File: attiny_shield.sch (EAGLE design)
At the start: 13 parts, among them IC1 TINY13-20PU

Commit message: - clean-up
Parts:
- 85_V_84: device SparkFun-Switches:SWITCH-SPDT-SMD-AYZ0202 -> PianoPiano:SPARKFUN-SWITCHES_SWITCH-SPDT-SMD-AYZ0202
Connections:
- removed net N$9: C1.1, PROGRAM_SWITCH.S
- new net N$1: C1.1, PROGRAM_SWITCH.O
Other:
- note added: "Arduino Uno R3"
- moved on the sheet: C1, J5, J6, J7, J8

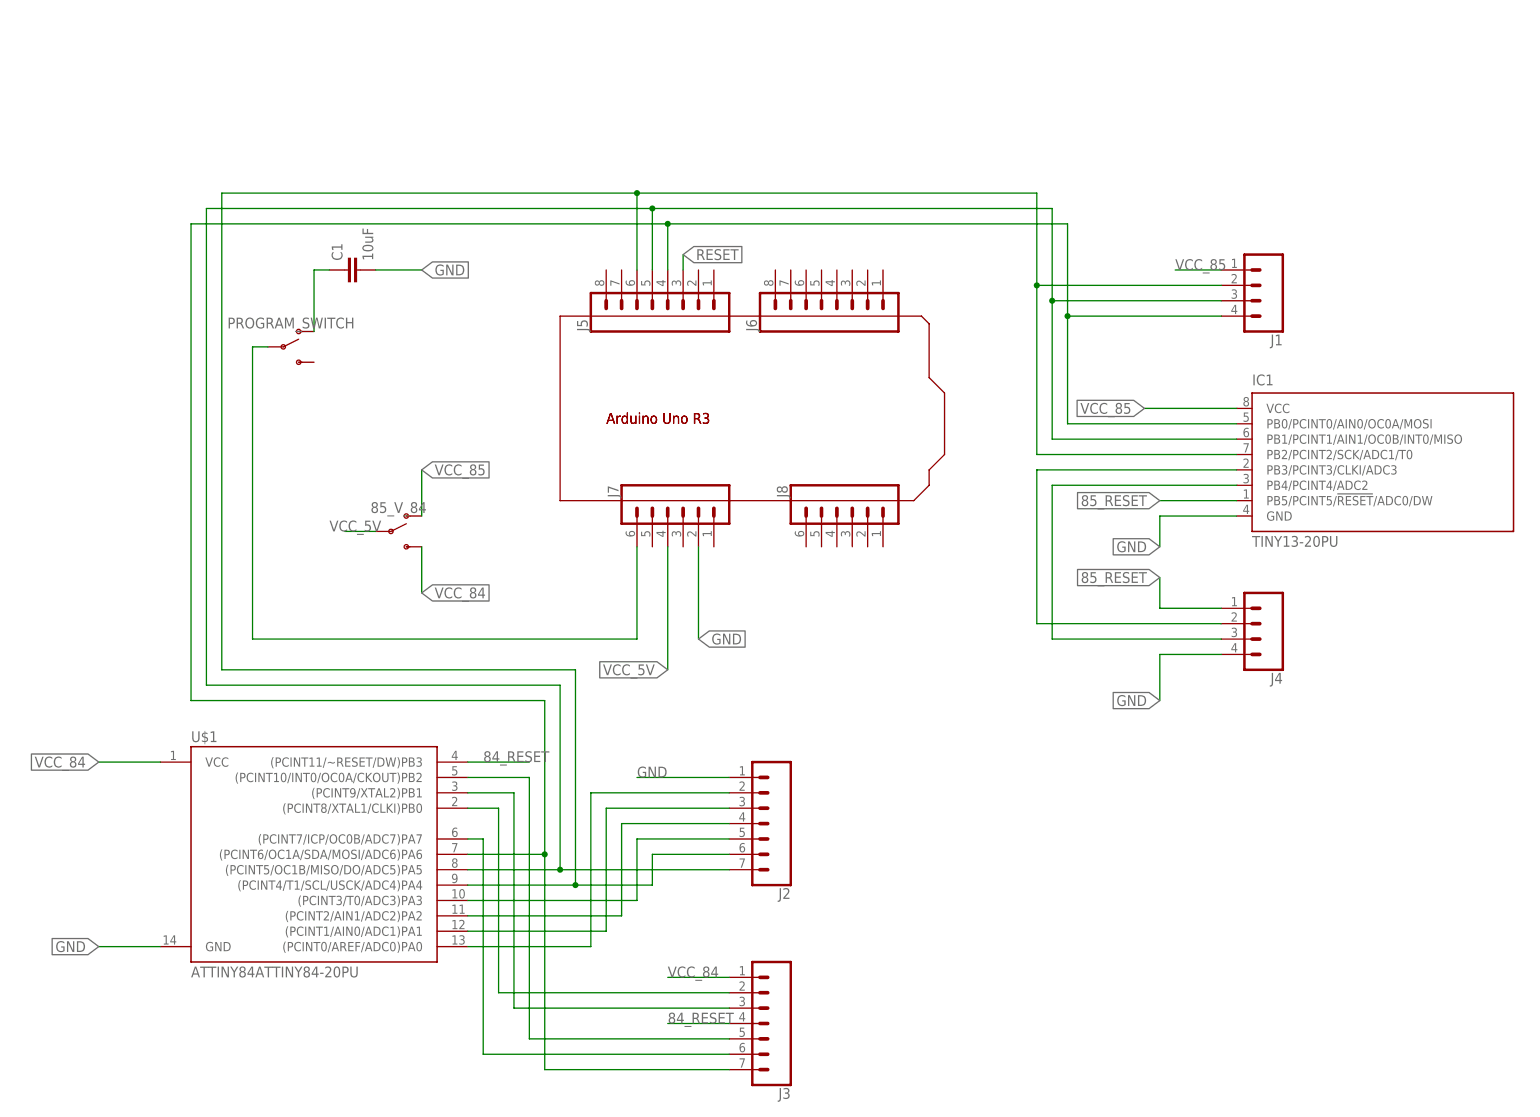
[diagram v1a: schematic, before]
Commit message: added caps and pull-ups. added reset button.
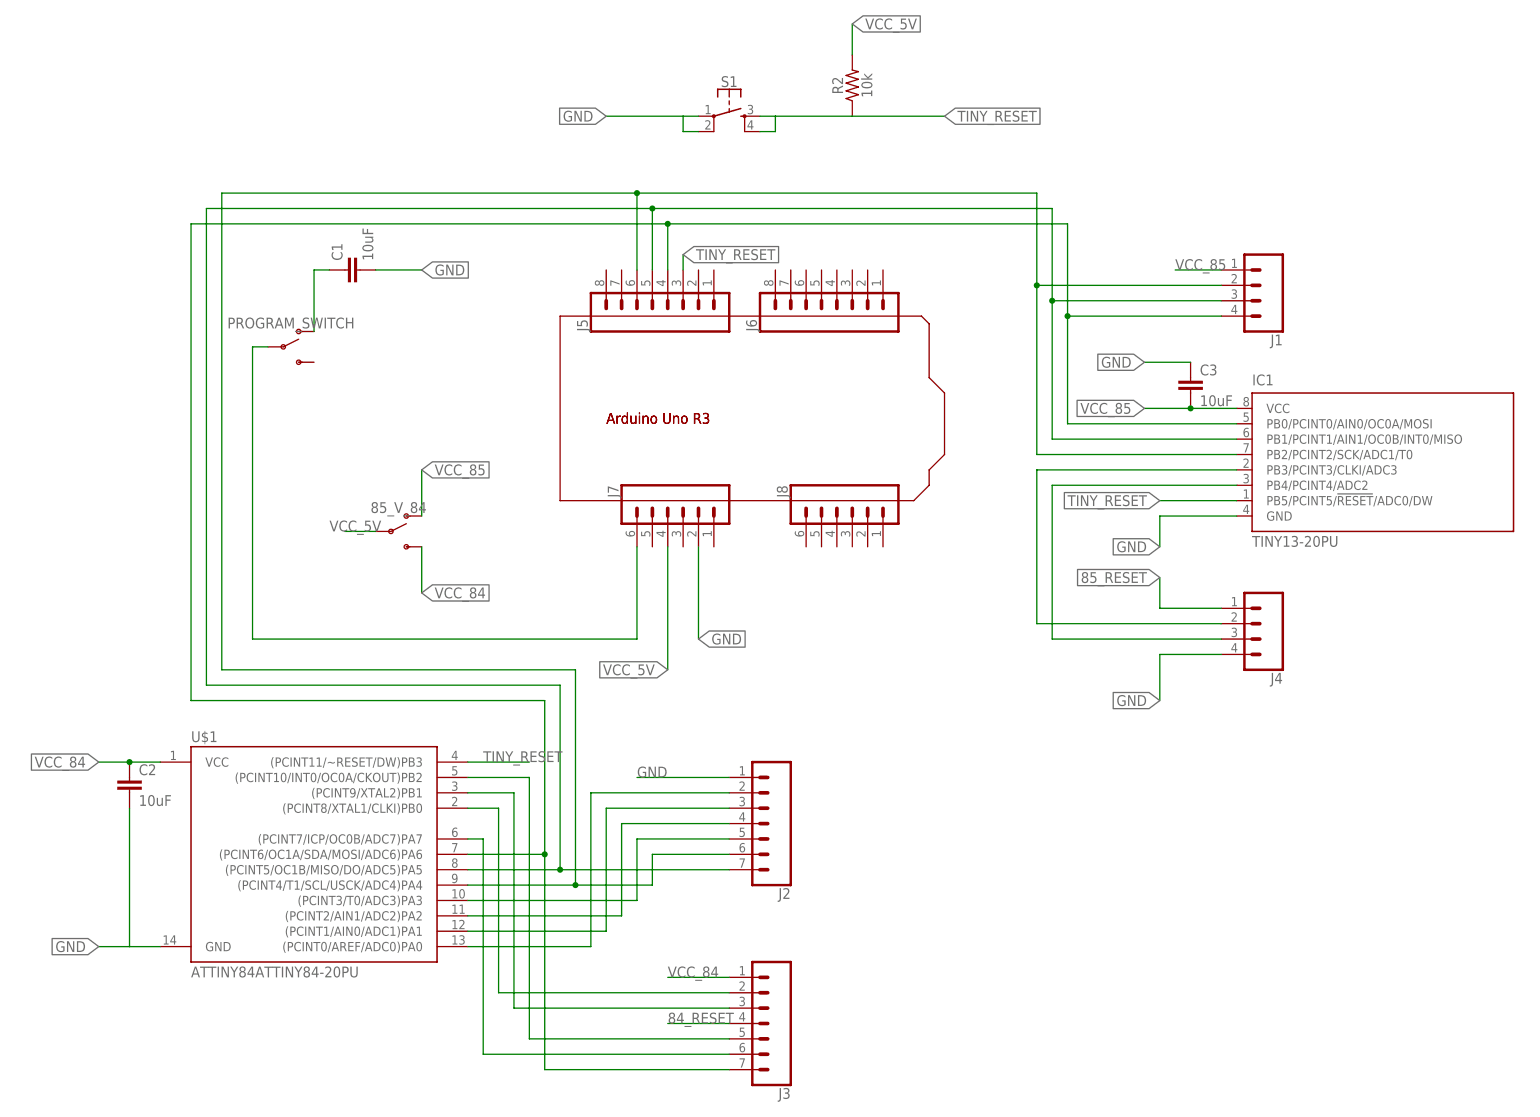
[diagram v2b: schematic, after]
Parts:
- added C2, C3: 10uF, SparkFun-Capacitors:10UF-0805-10V-10%
- added R2: 10k, PianoPiano:SPARKFUN-RESISTORS_10KOHM-0603-1/10W-1%
- added S1: (no value), PianoPiano:SPARKFUN-SWITCHES_MOMENTARY-SWITCH-SPST-2-SMD-5.2MM
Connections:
- removed net RESET: J5.3
- new net TINY_RESET: IC1.PB5/PCINT5/!RESET!/ADC0/DW, J5.3, R2.1, S1.3, S1.4, U$1.(PCINT11/~RESET/DW)PB3
- net 84_RESET: no longer U$1.(PCINT11/~RESET/DW)PB3
- net 85_RESET: no longer IC1.PB5/PCINT5/!RESET!/ADC0/DW
- net GND: now also C2.2, C3.1, S1.1, S1.2
- net VCC_5V: now also R2.2
- net VCC_84: now also C2.1
- net VCC_85: now also C3.2
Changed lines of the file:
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@@
 <drawing>
 <settings>
-<setting alwaysvectorfont="yes"/>
+<setting alwaysvectorfont="no"/>
 <setting verticaltext="up"/>
 </settings>
@@
 <part name="J7" library="SparkFun-Connectors" library_urn="urn:adsk.eagle:library:513" deviceset="CONN_06" device="SILK_FEMALE_PTH" package3d_urn="urn:adsk.eagle:package:38009/1"/>
 <part name="J8" library="SparkFun-Connectors" library_urn="urn:adsk.eagle:library:513" deviceset="CONN_06" device="SILK_FEMALE_PTH" package3d_urn="urn:adsk.eagle:package:38009/1"/>
+<part name="S1" library="PianoPiano" library_urn="urn:adsk.eagle:library:1762222" deviceset="SPARKFUN-SWITCHES_MOMENTARY-SWITCH-SPST-2" device="-SMD-5.2MM" package3d_urn="urn:adsk.eagle:package:1762345/2"/>
+<part name="R2" library="PianoPiano" library_urn="urn:adsk.eagle:library:1762222" deviceset="SPARKFUN-RESISTORS_10KOHM" device="-0603-1/10W-1%" package3d_urn="urn:adsk.eagle:package:1762339/2" value="10k"/>
+<part name="C2" library="SparkFun-Capacitors" deviceset="10UF" device="-0805-10V-10%" value="10uF"/>
+<part name="C3" library="SparkFun-Capacitors" deviceset="10UF" device="-0805-10V-10%" value="10uF"/>
 </parts>
 <sheets>
@@
 <instance part="J7" gate="G$1" x="55.88" y="106.68" rot="MR270"/>
 <instance part="J8" gate="G$1" x="83.82" y="106.68" rot="MR270"/>
+<instance part="S1" gate="G$1" x="63.5" y="172.72"/>
+<instance part="R2" gate="G$1" x="83.82" y="177.8" rot="R90"/>
+<instance part="C2" gate="G$1" x="-35.56" y="60.96"/>
+<instance part="C3" gate="G$1" x="139.7" y="127"/>
 </instances>
 <busses>
@@
 </segment>
 </net>
-<net name="RESET" class="0">
-<segment>
-<wire x1="55.88" y1="149.86" x2="55.88" y2="147.32" width="0.1524" layer="91"/>
-<label x="55.88" y="149.86" size="1.778" layer="95" xref="yes"/>
-<pinref part="J5" gate="G$1" pin="3"/>
-</segment>
-</net>
 <net name="VCC_85" class="0">
 <segment>
@@
 <segment>
 <pinref part="IC1" gate="G$1" pin="VCC"/>
-<wire x1="147.32" y1="124.46" x2="132.08" y2="124.46" width="0.1524" layer="91"/>
+<wire x1="147.32" y1="124.46" x2="139.7" y2="124.46" width="0.1524" layer="91"/>
 <label x="132.08" y="124.46" size="1.778" layer="95" rot="R180" xref="yes"/>
+<pinref part="C3" gate="G$1" pin="2"/>
+<wire x1="139.7" y1="124.46" x2="132.08" y2="124.46" width="0.1524" layer="91"/>
+<junction x="139.7" y="124.46"/>
 </segment>
 <segment>
@@
 <segment>
 <pinref part="U$1" gate="G$1" pin="GND"/>
-<wire x1="-30.48" y1="35.56" x2="-40.64" y2="35.56" width="0.1524" layer="91"/>
+<wire x1="-30.48" y1="35.56" x2="-35.56" y2="35.56" width="0.1524" layer="91"/>
 <label x="-40.64" y="35.56" size="1.778" layer="95" rot="R180" xref="yes"/>
+<pinref part="C2" gate="G$1" pin="2"/>
+<wire x1="-35.56" y1="35.56" x2="-40.64" y2="35.56" width="0.1524" layer="91"/>
+<wire x1="-35.56" y1="58.42" x2="-35.56" y2="35.56" width="0.1524" layer="91"/>
 </segment>
 <segment>
@@
 <label x="134.62" y="76.2" size="1.778" layer="95" rot="R180" xref="yes"/>
 </segment>
+<segment>
+<pinref part="S1" gate="G$1" pin="1"/>
+<wire x1="58.42" y1="172.72" x2="55.88" y2="172.72" width="0.1524" layer="91"/>
+<pinref part="S1" gate="G$1" pin="2"/>
+<wire x1="58.42" y1="170.18" x2="55.88" y2="170.18" width="0.1524" layer="91"/>
+<wire x1="55.88" y1="170.18" x2="55.88" y2="172.72" width="0.1524" layer="91"/>
+<wire x1="55.88" y1="172.72" x2="43.18" y2="172.72" width="0.1524" layer="91"/>
+<label x="43.18" y="172.72" size="1.778" layer="95" rot="R180" xref="yes"/>
+</segment>
+<segment>
+<pinref part="C3" gate="G$1" pin="1"/>
+<wire x1="139.7" y1="132.08" x2="132.08" y2="132.08" width="0.1524" layer="91"/>
+<label x="132.08" y="132.08" size="1.778" layer="95" rot="R180" xref="yes"/>
+</segment>
 </net>
 <net name="VCC_5V" class="0">
@@
 <label x="-2.54" y="104.14" size="1.778" layer="95"/>
 </segment>
+<segment>
+<pinref part="R2" gate="G$1" pin="2"/>
+<wire x1="83.82" y1="182.88" x2="83.82" y2="187.96" width="0.1524" layer="91"/>
+<label x="83.82" y="187.96" size="1.778" layer="95" xref="yes"/>
+</segment>
 </net>
 <net name="VCC_84" class="0">
 <segment>
 <pinref part="U$1" gate="G$1" pin="VCC"/>
-<wire x1="-40.64" y1="66.04" x2="-30.48" y2="66.04" width="0.1524" layer="91"/>
+<wire x1="-40.64" y1="66.04" x2="-35.56" y2="66.04" width="0.1524" layer="91"/>
 <label x="-40.64" y="66.04" size="1.778" layer="95" rot="R180" xref="yes"/>
+<pinref part="C2" gate="G$1" pin="1"/>
+<wire x1="-35.56" y1="66.04" x2="-30.48" y2="66.04" width="0.1524" layer="91"/>
+<junction x="-35.56" y="66.04"/>
 </segment>
 <segment>
@@
 <label x="53.34" y="22.86" size="1.778" layer="95"/>
 </segment>
-<segment>
-<pinref part="U$1" gate="G$1" pin="(PCINT11/~RESET/DW)PB3"/>
-<wire x1="30.48" y1="66.04" x2="20.32" y2="66.04" width="0.1524" layer="91"/>
-<label x="22.86" y="66.04" size="1.778" layer="95"/>
-</segment>
 </net>
 <net name="85_RESET" class="0">
@@
 <label x="134.62" y="96.52" size="1.778" layer="95" rot="R180" xref="yes"/>
 </segment>
-<segment>
-<pinref part="IC1" gate="G$1" pin="PB5/PCINT5/!RESET!/ADC0/DW"/>
-<wire x1="134.62" y1="109.22" x2="147.32" y2="109.22" width="0.1524" layer="91"/>
-<label x="134.62" y="109.22" size="1.778" layer="95" rot="R180" xref="yes"/>
-</segment>
 </net>
 <net name="N$1" class="0">
@@
 </segment>
 </net>
+<net name="TINY_RESET" class="0">
+<segment>
+<pinref part="U$1" gate="G$1" pin="(PCINT11/~RESET/DW)PB3"/>
+<wire x1="30.48" y1="66.04" x2="20.32" y2="66.04" width="0.1524" layer="91"/>
+<label x="22.86" y="66.04" size="1.778" layer="95"/>
+</segment>
+<segment>
+<pinref part="IC1" gate="G$1" pin="PB5/PCINT5/!RESET!/ADC0/DW"/>
+<wire x1="134.62" y1="109.22" x2="147.32" y2="109.22" width="0.1524" layer="91"/>
+<label x="134.62" y="109.22" size="1.778" layer="95" rot="R180" xref="yes"/>
+</segment>
+<segment>
+<wire x1="55.88" y1="149.86" x2="55.88" y2="147.32" width="0.1524" layer="91"/>
+<label x="55.88" y="149.86" size="1.778" layer="95" xref="yes"/>
+<pinref part="J5" gate="G$1" pin="3"/>
+</segment>
+<segment>
+<pinref part="S1" gate="G$1" pin="3"/>
+<wire x1="68.58" y1="172.72" x2="71.12" y2="172.72" width="0.1524" layer="91"/>
+<pinref part="S1" gate="G$1" pin="4"/>
+<wire x1="71.12" y1="172.72" x2="83.82" y2="172.72" width="0.1524" layer="91"/>
+<wire x1="68.58" y1="170.18" x2="71.12" y2="170.18" width="0.1524" layer="91"/>
+<wire x1="71.12" y1="170.18" x2="71.12" y2="172.72" width="0.1524" layer="91"/>
+<pinref part="R2" gate="G$1" pin="1"/>
+<wire x1="83.82" y1="172.72" x2="99.06" y2="172.72" width="0.1524" layer="91"/>
+<label x="99.06" y="172.72" size="1.778" layer="95" xref="yes"/>
+</segment>
+</net>
